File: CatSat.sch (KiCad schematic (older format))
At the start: 0 parts

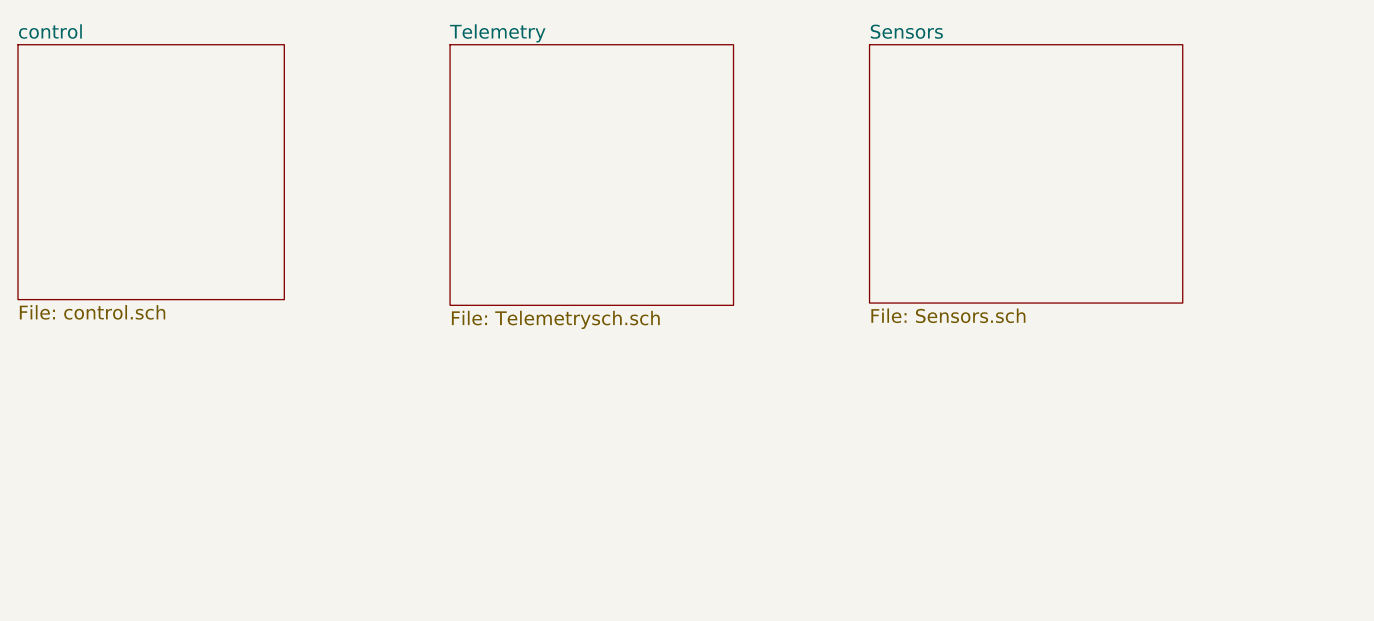
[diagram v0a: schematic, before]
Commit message: Schematic v0.2
Added IC and wiring
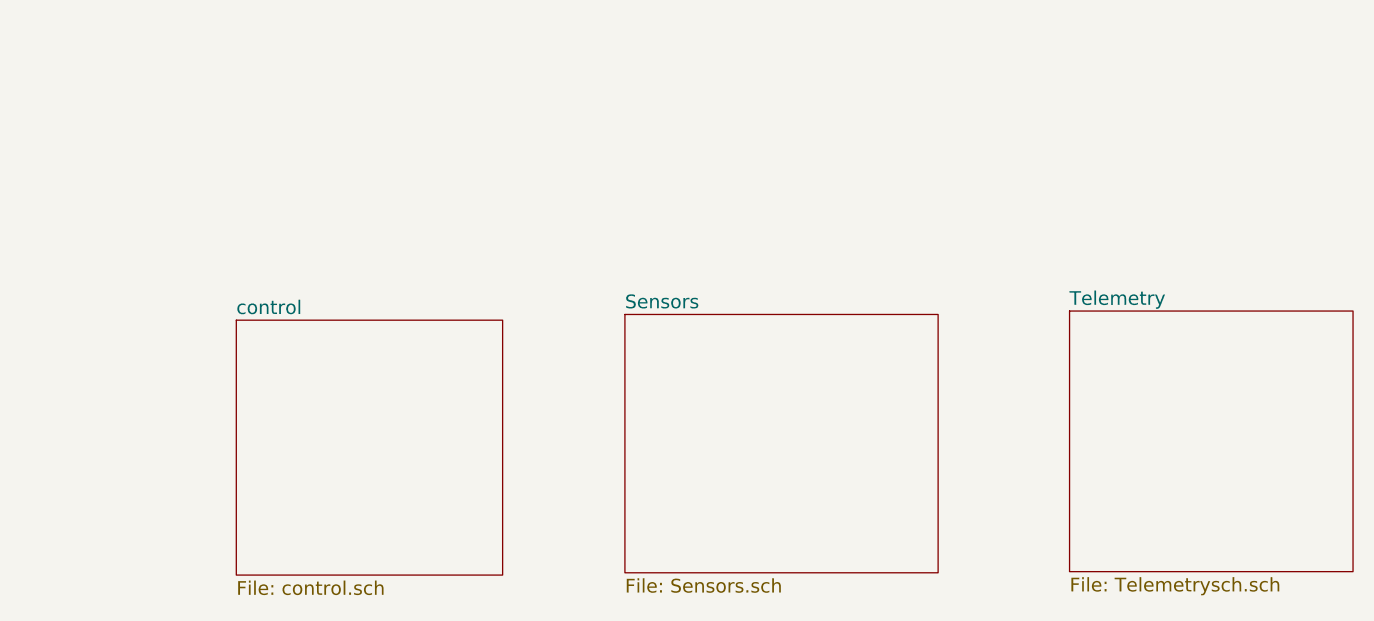
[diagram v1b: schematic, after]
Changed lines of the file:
@@
 LIBS:L80-M39
 LIBS:RFM95W-868S2
+LIBS:theinventorhouse
 LIBS:CatSat-cache
 EELAYER 25 0
@@
 $EndDescr
 $Sheet
-S 2510 2275 1165 1115
+S 3465 3480 1165 1115
 U 57965E31
 F0 "control" 60
@@
 $EndSheet
 $Sheet
-S 4400 2275 1240 1140
+S 7110 3440 1240 1140
 U 57965E45
 F0 "Telemetry" 60
@@
 $EndSheet
 $Sheet
-S 6235 2275 1370 1130
+S 5165 3455 1370 1130
 U 57965E56
 F0 "Sensors" 60
